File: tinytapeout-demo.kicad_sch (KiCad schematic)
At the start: 137 parts, among them J1 Conn_01x06, J12 613012243121, J13 613012243121, J14 613012243121, J15 USB4500-03-0-A_REVA, J16 2x20_P2.54mm_Pinheader, J17 Conn_01x03, J18 2x20_P2.54mm_Pinheader, J19 Conn_01x02, J2 Conn_01x04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

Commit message: v3p5 pcba BOM tweaks
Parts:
- D1, D2, D3, D4: Characteristics Yellow LED -> Yellow LED, Low 1.8 V Vf; MPN LTST-C190YKT -> CSL1901YW1; MPN_ALT TLMY1000-GS15 -> LY L29K-H1K2-26-Z
- J15: MANUFACTURER GCT -> (none); MAXIMUM_PACKAGE_HEIGHT 2.46mm -> (none)
- J3, J5, J6: now not fitted
- R22, R23, R24, R25, R26, R27, R28, R29: value 68R -> 510; Characteristics 68R 0402 -> 510R 0402; MPN RC0402FR-0768RL -> RC0402FR-07510RL; MPN_ALT WR04X68R0FTL -> CR0402-FX-5100GLF
- U7: Characteristics (none) -> FLASHED FOR CARAVEL; now fitted
- X1: Characteristics (none) -> 20MHz osc; DigikeyPN 1923-830208220401DKR-ND -> 1923-830208220401CT-ND; MPN_ALT (none) -> 831056293; Part number 830208220401 -> (none)
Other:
- note added: "E.g. if you wanted an SPI controlled periph as part of your TT project, you could configure it such that it uses: in[0] as select/~{cs} in[1] for clocking in[2] for tx/mosi and out[3] for rx/miso"
- note added: "Tiny Tapeout 4/5 Demo Board"
- note removed: "E.g. if you wanted an SPI controlled periphas part of your TT project, you could configure it such that it uses: in[0] as select/~{cs} in[1] for clocking in[2] for tx/mosi and out[3] for rx/miso"
- note removed: "TinyTapeout 4/5 Demo Board"

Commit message: v1.1.1 compliance with newspeak is double-plus-good
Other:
- note added: "E.g. if you wanted an SPI controlled periph as part of your TT project, you could configure it such that it uses: in[0] as select/~{cs} in[1] for clocking in[2] for tx/copi and out[3] for rx/cipo"
- note added: "PMOD, specialized versions. These PMODs offer an array of options while attempting to keep to standard digilent pinouts. With "SPI Periph", the pmod controls the bus and the project responds. On "SPI Control", the pmod is a peripheral device to the project. The bidir/uart header is flexible."
- note added: "SPI Control/I2C"
- note added: "SPI Periph"
- note added: "ci"
- note added: "cipo"
- note added: "co"
- note added: "copi"
- note removed: "E.g. if you wanted an SPI controlled periph as part of your TT project, you could configure it such that it uses: in[0] as select/~{cs} in[1] for clocking in[2] for tx/mosi and out[3] for rx/miso"
- note removed: "PMOD, specialized versions. These PMODs offer an array of options while attempting to keep to standard digilent pinouts. With "SPI Slave", the pmod controls the bus and the project responds. On "SPI Master", the pmod is a peripheral device to the project. The bidir/uart header is flexible."
- note removed: "SPI Master/I2C"
- note removed: "SPI Slave"
- note removed: "miso"
- note removed: "mosi"
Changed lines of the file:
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@@
 	(title_block
 		(title "TinyTapeout 4/5 Demo Board")
-		(date "2024-02-29")
-		(rev "1.1.0")
+		(date "2024-03-12")
+		(rev "1.1.1")
 		(company "Psychogenic Technologies")
 		(comment 1 "(C) 2023, 2024 Pat Deegan")
@@
 		)
 	)
-	(text "mo"
+	(text "co"
 		(exclude_from_sim no)
 		(at 269.24 259.08 0)
@@
 		)
 	)
-	(text "SPI Master/I2C"
+	(text "SPI Control/I2C"
 		(exclude_from_sim no)
 		(at 242.57 240.03 0)
@@
 		)
 	)
-	(text "mo"
+	(text "co"
 		(exclude_from_sim no)
 		(at 177.8 259.08 0)
@@
 		)
 	)
-	(text "miso"
+	(text "cipo"
 		(exclude_from_sim no)
 		(at 220.726 256.286 0)
@@
 	(text "Output PMOD"
 		(exclude_from_sim no)
-		(at 111.76 238.76 0)
+		(at 115.062 241.554 0)
 		(effects
 			(font
@@
 		)
 	)
-	(text "SPI Slave"
+	(text "SPI Periph"
 		(exclude_from_sim no)
 		(at 179.07 240.03 0)
@@
 		)
 	)
-	(text "mi"
+	(text "ci"
 		(exclude_from_sim no)
 		(at 269.24 256.54 0)
@@
 		)
 	)
-	(text "mi"
+	(text "ci"
 		(exclude_from_sim no)
 		(at 177.8 256.54 0)
@@
 		)
 	)
-	(text "E.g. if you wanted an SPI controlled\nperiph as part of your TT project, you \ncould configure it such that it uses:\nin[0] as select/~{cs}\nin[1] for clocking\nin[2] for tx/mosi\nand \nout[3] for rx/miso"
+	(text "E.g. if you wanted an SPI controlled\nperiph as part of your TT project, you \ncould configure it such that it uses:\nin[0] as select/~{cs}\nin[1] for clocking\nin[2] for tx/copi\nand \nout[3] for rx/cipo"
 		(exclude_from_sim no)
 		(at 198.755 182.245 0)
@@
 		)
 	)
-	(text "PMOD, specialized versions.  These PMODs    offer an array of options while attempting to keep to\nstandard digilent pinouts.  With \"SPI Slave\", the pmod controls the bus and the project responds.\nOn \"SPI Master\", the pmod is a peripheral device to the project.  The bidir/uart header is flexible.\n"
+	(text "PMOD, specialized versions.  These PMODs    offer an array of options while attempting to keep to\nstandard digilent pinouts.  With \"SPI Periph\", the pmod controls the bus and the project responds.\nOn \"SPI Control\", the pmod is a peripheral device to the project.  The bidir/uart header is flexible.\n"
 		(exclude_from_sim no)
 		(at 168.91 280.67 0)
@@
 		)
 	)
-	(text "mosi"
+	(text "copi"
 		(exclude_from_sim no)
 		(at 220.98 259.08 0)

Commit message: v1.1.1 docs
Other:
- title: TinyTapeout 4/5 Demo Board -> Tiny Tapeout 4/5 Demo Board
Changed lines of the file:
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@@
 	(paper "A3")
 	(title_block
-		(title "TinyTapeout 4/5 Demo Board")
+		(title "Tiny Tapeout 4/5 Demo Board")
 		(date "2024-03-12")
 		(rev "1.1.1")

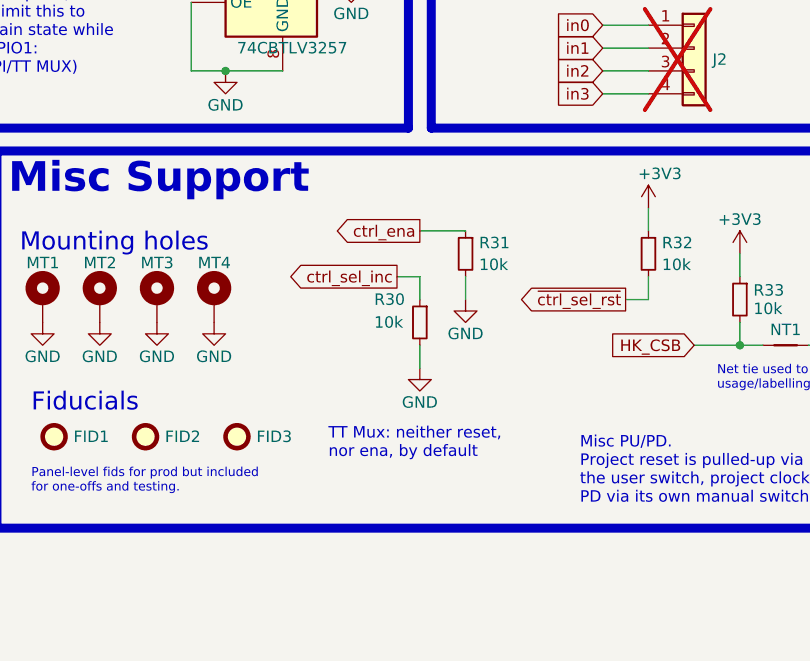
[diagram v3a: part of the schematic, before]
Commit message: JLC MPNs, mux ctrl ena pullup fix
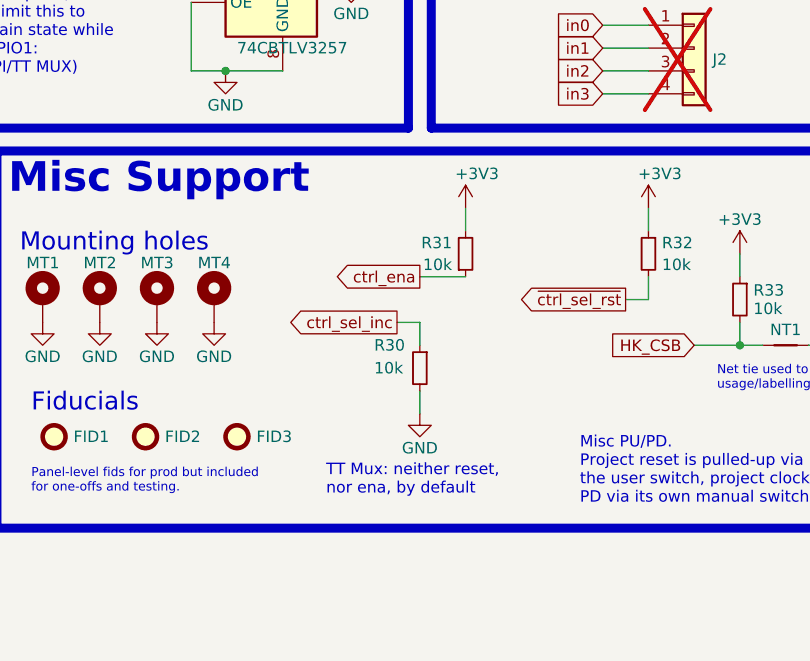
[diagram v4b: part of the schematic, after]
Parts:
- C1, C11, C15, C17, C25, C42, C48, C49, C5, C57, C59, C61, C9: JLC (none) -> C5673
- C12, C13, C14, C18, C19, C2, C20, C22, C23, C24, C26, C27, C28, C4, C43, C56, C58, C60, C8: JLC (none) -> C100072
- C16, C21: JLC (none) -> C962136
- C44, C45, C46, C47: JLC (none) -> C107005
- D5, D6: JLC (none) -> C6961594; MPN_ALT (none) -> C6961594
- F2: JLC (none) -> C3760470
- FB1: JLC (none) -> C2649119
- J12, J13, J14, J3, J5, J6: JLC (none) -> C6147817
- J15: JLC (none) -> C7407287; MPN_ALT (none) -> USB4500-03-1-A
- J16, J18: JLC (none) -> C3294478; MPN_ALT M20-8762042 -> PZ254-2-20-S
- J4: Characteristics (none) -> Virtual part, attached to board via J16, J18; DigikeyPN 609-3124-ND x 2 -> (none); MPN 95157-440LF x 2 -> (none); now left out of the parts list
- R1, R10, R11, R13, R14, R2, R3, R4, R5, R6: JLC (none) -> C202394
- R12, R30, R31, R32, R33, R42, R43, R44, R45, R46, R47, R48, R8, R9: JLC (none) -> C471764
- R15: JLC (none) -> C138040
- R16: JLC (none) -> C858907
- R17, R19, R22, R23, R24, R25, R26, R27, R28, R29: JLC (none) -> C276273
- R18, R49: Characteristics 0R 0402 -> 0R 0603; JLC (none) -> C95177; MPN RC0402FR-070RL -> RC0603JR-070RL; MPN_ALT WR04X000 PTL -> (none)
- R20, R21: JLC (none) -> C138073
- R41: JLC (none) -> C4271317
- R7: JLC (none) -> C327139
- SW1, SW2, SW3: JLC (none) -> C5525525
- SW4: JLC (none) -> C2842673
- U1: JLC (none) -> C6976938
- U2: JLC (none) -> C15578
- U3: JLC (none) -> C176944
- U4: JLC (none) -> C546455
- U7: JLC (none) -> C82344
- X1: JLC (none) -> C17613581
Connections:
- net +3V3: now also R31.2
- net GND: no longer R31.2
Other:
- moved on the sheet: R30

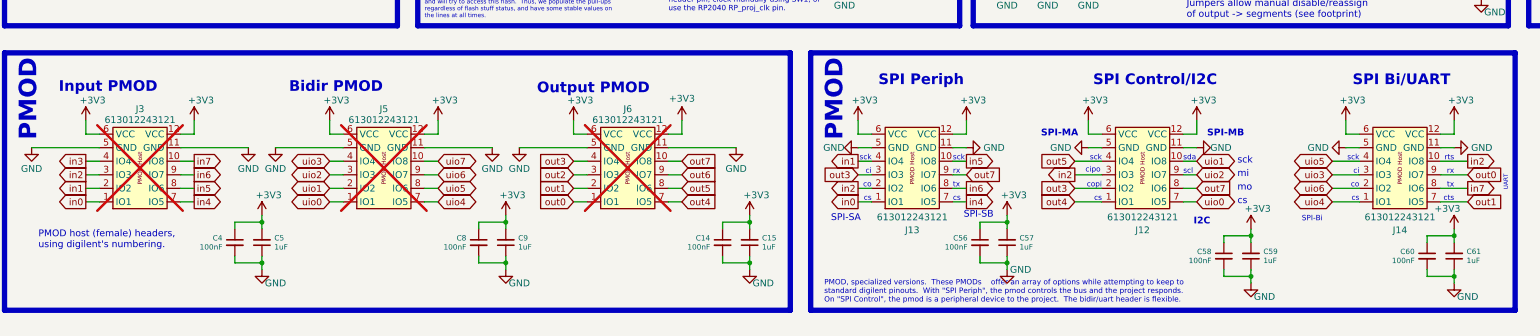
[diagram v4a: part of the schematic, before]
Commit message: PMOD header DNP swap/fix
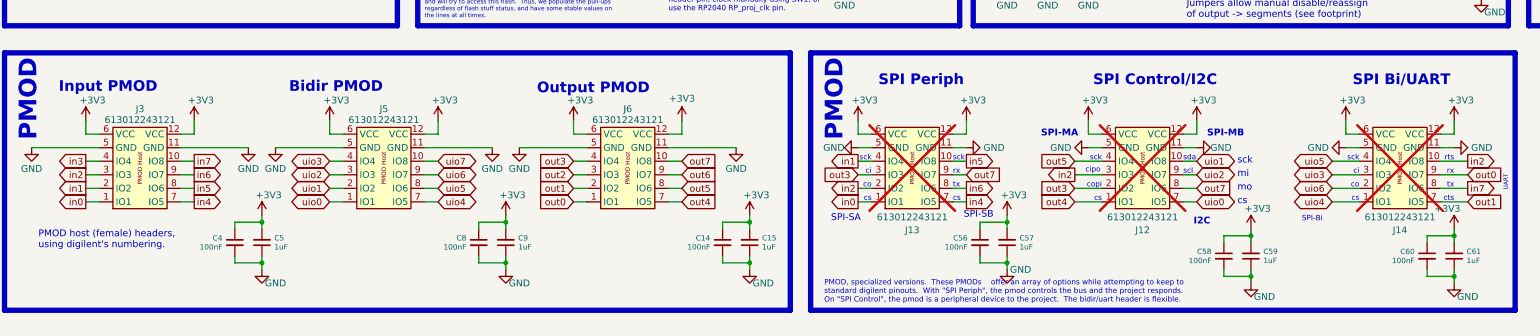
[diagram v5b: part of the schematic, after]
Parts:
- J12, J13, J14: now not fitted
- J3, J5, J6: now fitted
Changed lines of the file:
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@@
 		(in_bom yes)
 		(on_board yes)
-		(dnp yes)
+		(dnp no)
 		(fields_autoplaced yes)
 		(property "Reference" "J6"
@@
 		(in_bom yes)
 		(on_board yes)
-		(dnp no)
+		(dnp yes)
 		(property "Reference" "J14"
 			(at 276.86 266.9073 0)
@@
 			)
 		)
+		(property "Characteristics" ""
+			(at 276.86 251.46 0)
+			(effects
+				(font
+					(size 1.27 1.27)
+				)
+				(hide yes)
+			)
+		)
+		(property "Variant" ""
+			(at 276.86 251.46 0)
+			(effects
+				(font
+					(size 1.27 1.27)
+				)
+				(hide yes)
+			)
+		)
+		(property "DigikeyPN" ""
+			(at 276.86 251.46 0)
+			(effects
+				(font
+					(size 1.27 1.27)
+				)
+				(hide yes)
+			)
+		)
 		(pin "1"
 		)
@@
 		(in_bom yes)
 		(on_board yes)
-		(dnp no)
+		(dnp yes)
 		(property "Reference" "J13"
 			(at 185.42 266.9073 0)
@@
 		(in_bom yes)
 		(on_board yes)
-		(dnp yes)
+		(dnp no)
 		(fields_autoplaced yes)
 		(property "Reference" "J3"
@@
 		(in_bom yes)
 		(on_board yes)
-		(dnp yes)
+		(dnp no)
 		(fields_autoplaced yes)
 		(property "Reference" "J5"
@@
 		(in_bom yes)
 		(on_board yes)
-		(dnp no)
+		(dnp yes)
 		(property "Reference" "J12"
 			(at 228.6 266.9073 0)
@@
 			(at 228.6 251.46 0)
 			(effects
+				(font
+					(size 1.27 1.27)
+				)
+				(hide yes)
+			)
+		)
+		(property "Characteristics" ""
+			(at 228.6 251.46 0)
+			(effects
+				(font
+					(size 1.27 1.27)
+				)
+				(hide yes)
+			)
+		)
+		(property "Variant" ""
+			(at 228.6 251.46 0)
+			(effects
+				(font
+					(size 1.27 1.27)
+				)
+				(hide yes)
+			)
+		)
+		(property "DigikeyPN" ""
+			(at 228.6 251.46 0)
+			(effects

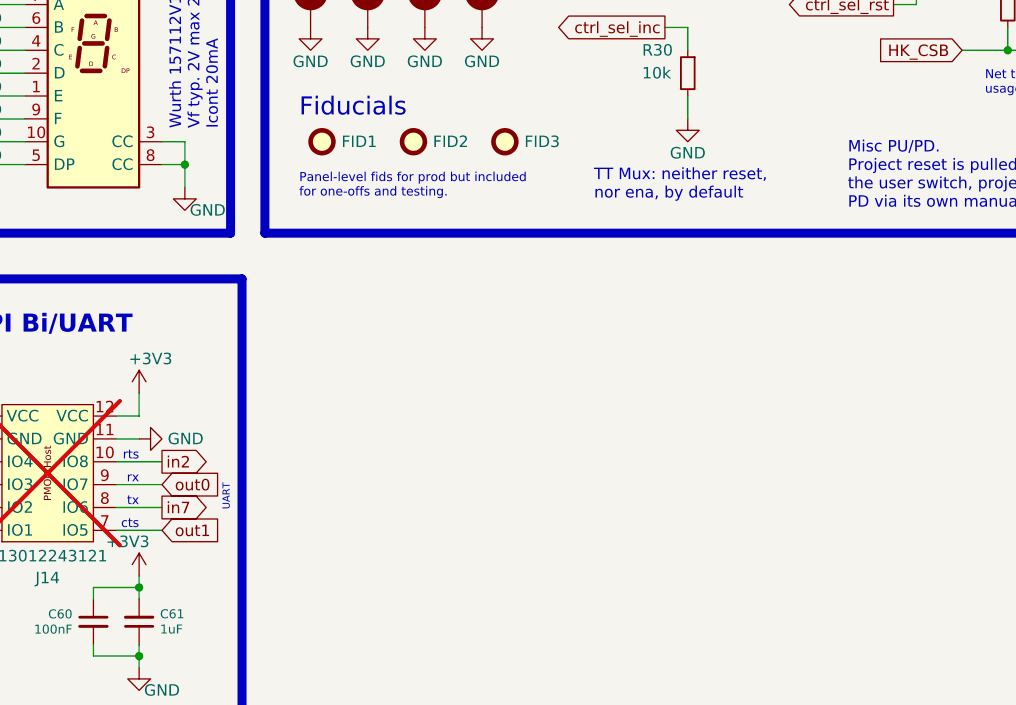
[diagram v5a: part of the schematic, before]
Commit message: UART pmod fix, minor routing and silk cleanups
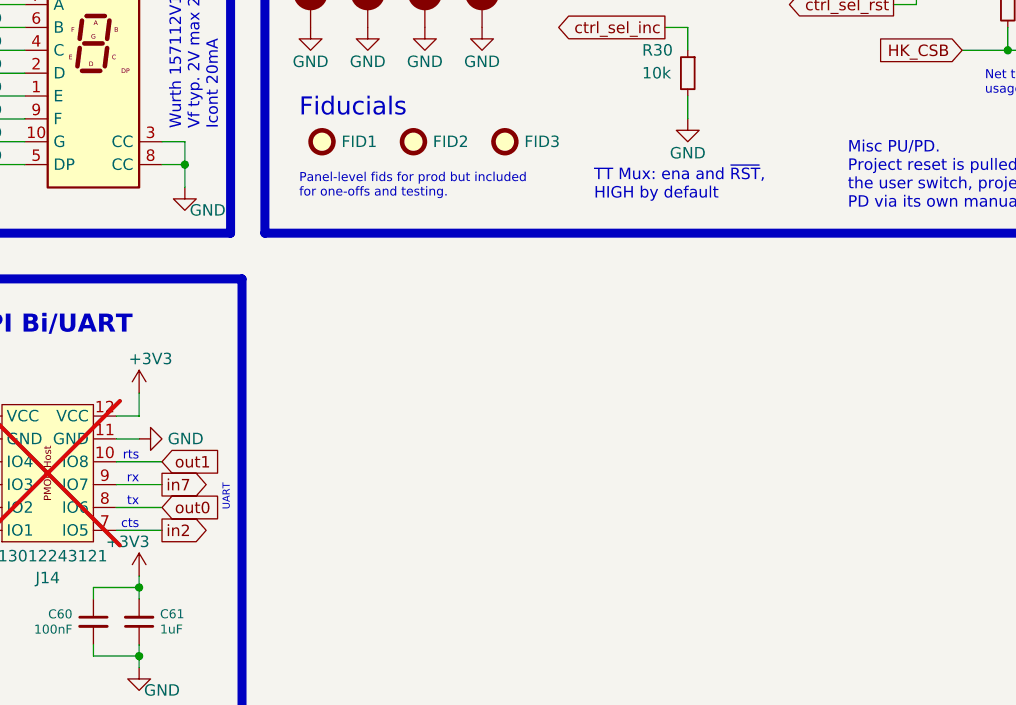
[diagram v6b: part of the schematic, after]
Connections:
- net in2: now also J14.7 (IO5); no longer J14.10 (IO8)
- net in7: now also J14.9 (IO7); no longer J14.8 (IO6)
- net out0: now also J14.8 (IO6); no longer J14.9 (IO7)
- net out1: now also J14.10 (IO8); no longer J14.7 (IO5)
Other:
- note added: "TT Mux: ena and ~{RST}, HIGH by default"
- note removed: "TT Mux: neither reset, nor ena, by default"
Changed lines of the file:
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@@
 	(title_block
 		(title "Tiny Tapeout 4/5 Demo Board")
-		(date "2024-04-10")
-		(rev "1.1.2")
+		(date "2024-04-11")
+		(rev "1.2.0")
 		(company "Psychogenic Technologies")
 		(comment 1 "(C) 2023, 2024 Pat Deegan")
@@
 		)
 	)
-	(text "TT Mux: neither reset, \nnor ena, by default"
+	(text "TT Mux: ena and ~{RST}, \nHIGH by default"
 		(exclude_from_sim no)
 		(at 337.566 225.044 0)
@@
 	(global_label "out0"
 		(shape input)
-		(at 289.56 256.54 0)
+		(at 289.56 259.08 0)
 		(fields_autoplaced yes)
 		(effects
@@
 		)
 		(property "Intersheetrefs" "${INTERSHEET_REFS}"
-			(at 296.7784 256.54 0)
+			(at 296.7784 259.08 0)
 			(effects
 				(font
@@
 	(global_label "out1"
 		(shape input)
-		(at 289.56 261.62 0)
+		(at 289.56 254 0)
 		(fields_autoplaced yes)
 		(effects
@@
 		)
 		(property "Intersheetrefs" "${INTERSHEET_REFS}"
-			(at 296.7784 261.62 0)
+			(at 296.7784 254 0)
 			(effects
 				(font
@@
 	(global_label "in7"
 		(shape output)
-		(at 289.56 259.08 0)
+		(at 289.56 256.54 0)
 		(fields_autoplaced yes)
 		(effects
@@
 		)
 		(property "Intersheetrefs" "${INTERSHEET_REFS}"
-			(at 295.5085 259.08 0)
+			(at 295.5085 256.54 0)
 			(effects
 				(font
@@
 	(global_label "in2"
 		(shape output)
-		(at 289.56 254 0)
+		(at 289.56 261.62 0)
 		(fields_autoplaced yes)
 		(effects
@@
 		)
 		(property "Intersheetrefs" "${INTERSHEET_REFS}"
-			(at 295.5085 254 0)
+			(at 295.5085 261.62 0)
 			(effects
 				(font
